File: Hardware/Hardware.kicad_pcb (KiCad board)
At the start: 2 copper layers, 68 parts, among them J1 LLINEIN, J2 RLINEIN, J3 MICIN, J4 Raspberry_Pi_2_3, J5 LOUT, J6 ROUT, J7 LHPOUT, J8 RHPOUT, SW1 JS5208, U1 MCP3004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

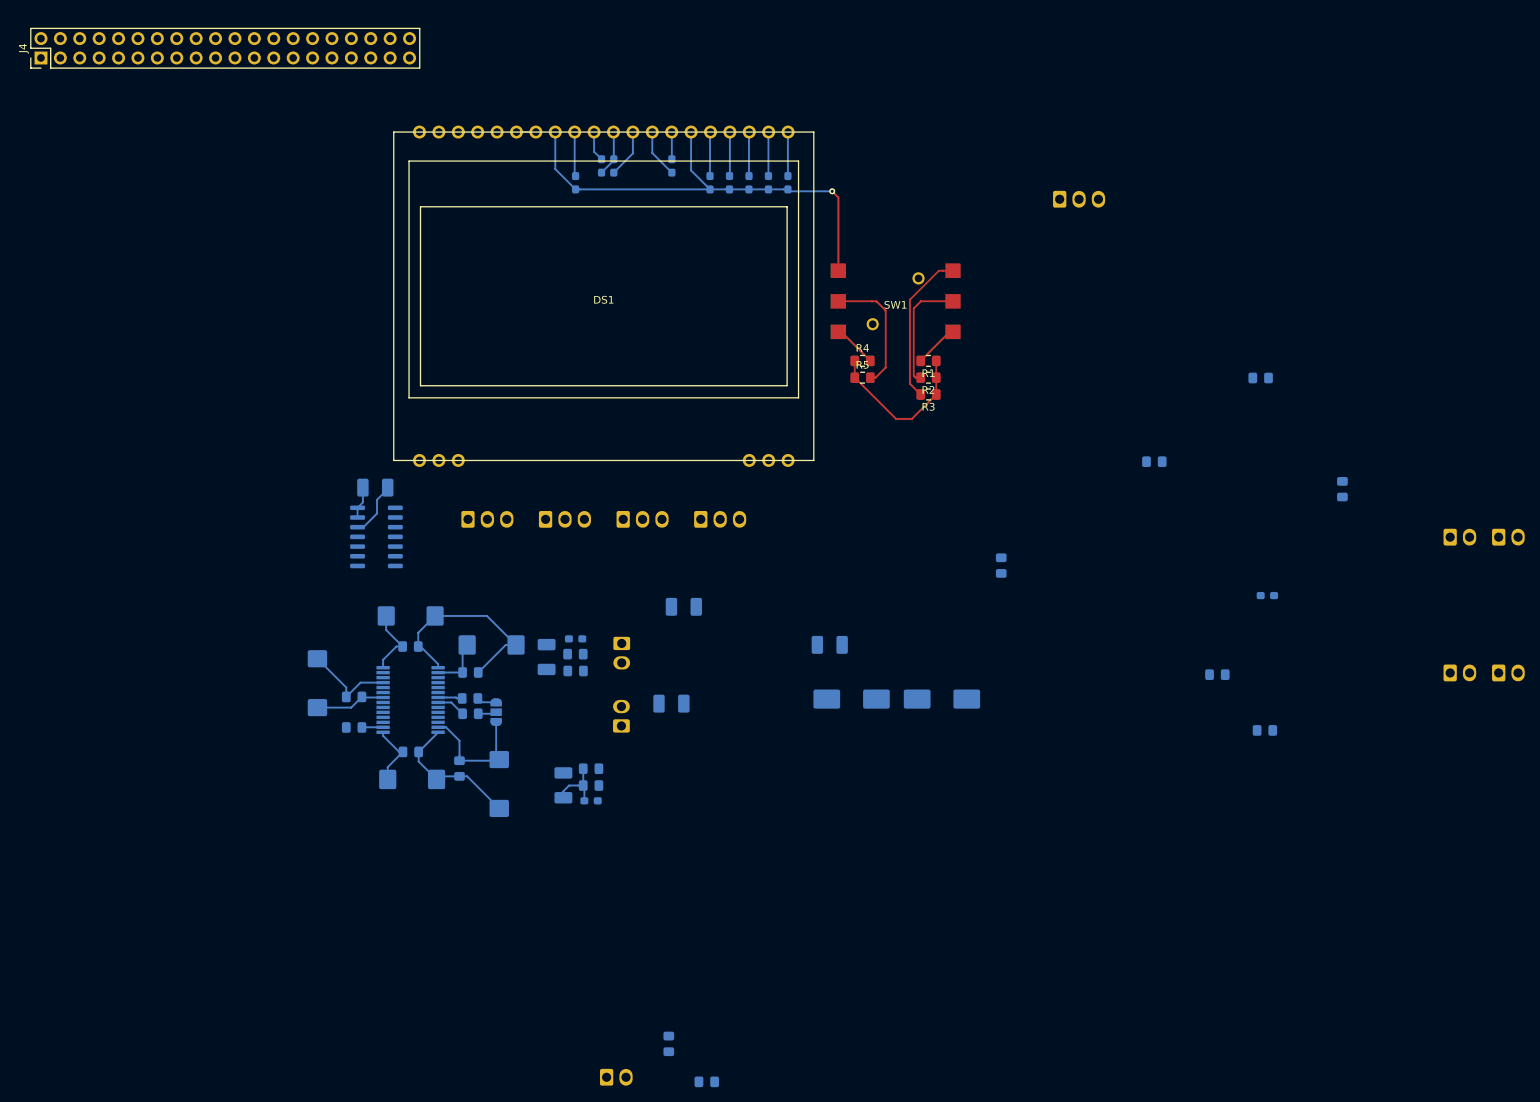
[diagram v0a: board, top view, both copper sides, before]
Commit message: Began layout and routing of PCB, generated files to allow use of FreeRouting
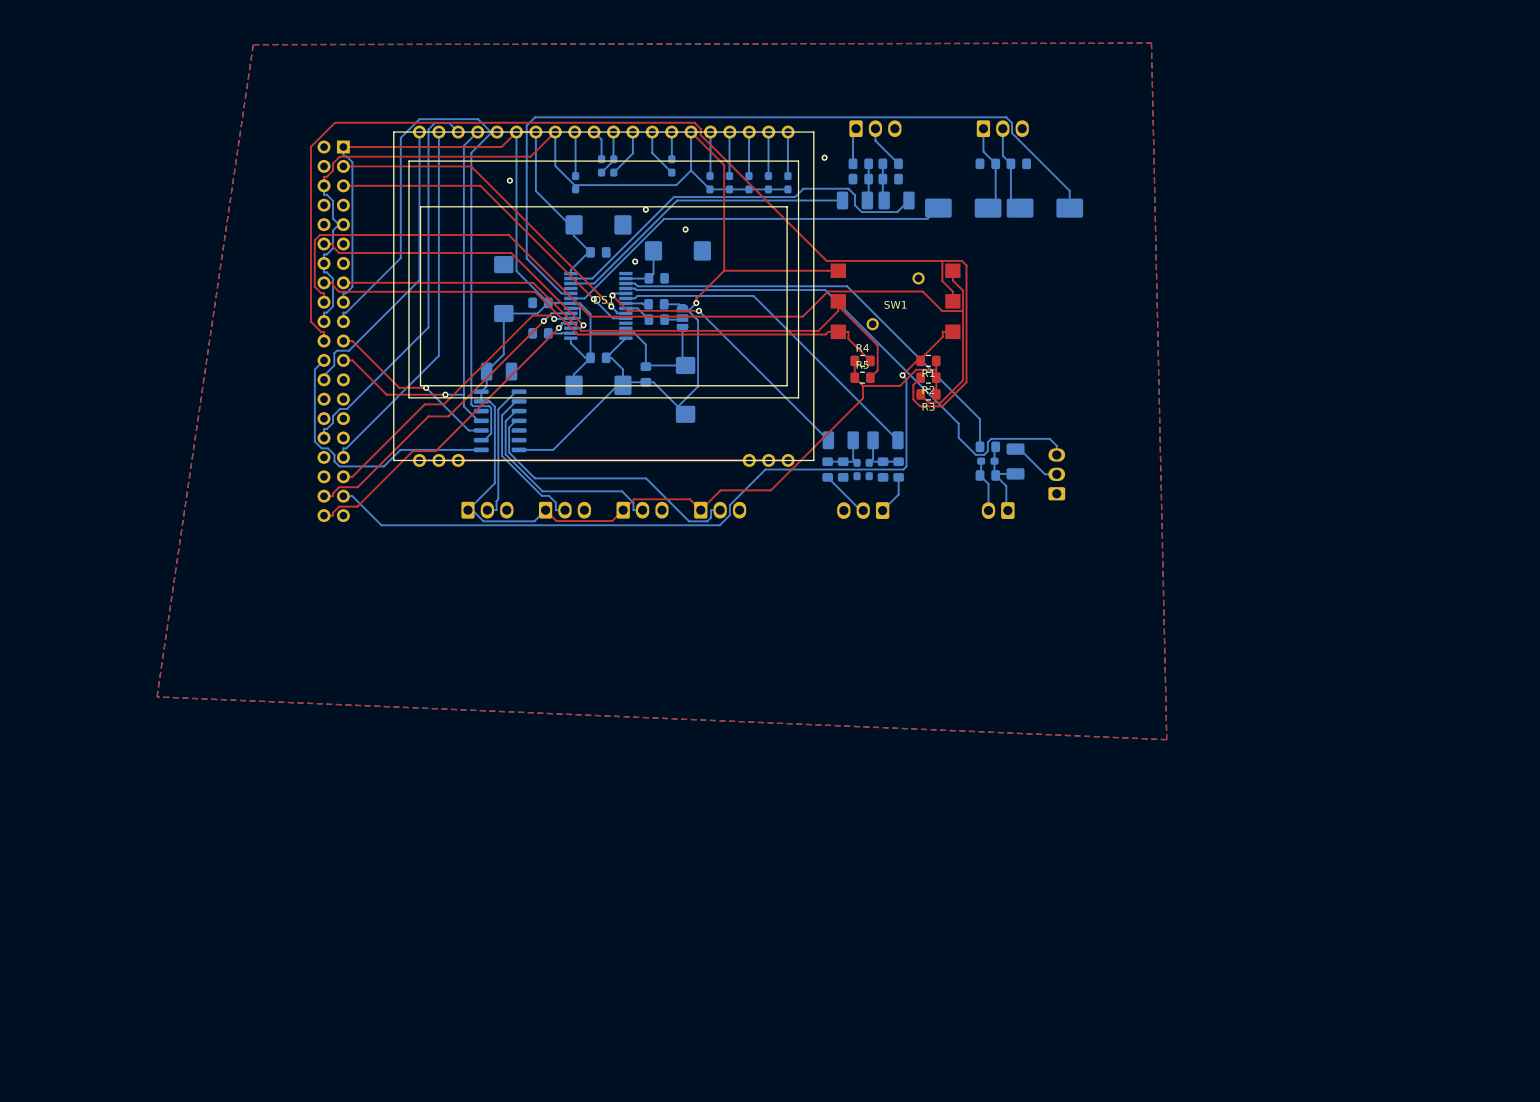
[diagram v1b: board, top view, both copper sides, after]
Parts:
- removed J6: ROUT, Connector_Molex:Molex_KK-254_AE-6410-02A_1x02_P2.54mm_Vertical
- removed J7: LHPOUT, Connector_Molex:Molex_KK-254_AE-6410-02A_1x02_P2.54mm_Vertical
- removed J8: RHPOUT, Connector_Molex:Molex_KK-254_AE-6410-02A_1x02_P2.54mm_Vertical
- J1: value LLINEIN -> LINEIN; footprint Connector_Molex:Molex_KK-254_AE-6410-02A_1x02_P2.54mm_Vertical -> Connector_Molex:Molex_KK-254_AE-6410-03A_1x03_P2.54mm_Vertical
- J2: value RLINEIN -> MICIN
- J3: value MICIN -> Raspberry_Pi_2_3; footprint Connector_Molex:Molex_KK-254_AE-6410-02A_1x02_P2.54mm_Vertical -> Connector_PinHeader_2.54mm:PinHeader_2x20_P2.54mm_Vertical
- J4: value Raspberry_Pi_2_3 -> LOUT; footprint Connector_PinHeader_2.54mm:PinHeader_2x20_P2.54mm_Vertical -> Connector_Molex:Molex_KK-254_AE-6410-03A_1x03_P2.54mm_Vertical; moved to B.Cu
- J5: value LOUT -> HPOUT; footprint Connector_Molex:Molex_KK-254_AE-6410-02A_1x02_P2.54mm_Vertical -> Connector_Molex:Molex_KK-254_AE-6410-03A_1x03_P2.54mm_Vertical
- moved J3 126.6 mm to (76.4, 33.8), turned to 180 degrees
- moved J4 107.1 mm to (143.5, 31.4), turned to 0 degrees
- moved R11 90.9 mm to (160.8, 73.1), turned to 180 degrees
- moved R16 87.2 mm to (148.1, 38.0)
- moved R6 85.3 mm to (160.8, 76.8), turned to 180 degrees
- moved J5 81.2 mm to (160.2, 31.4)
- moved R15 79.9 mm to (144.1, 38.0), turned to 180 degrees
- moved R20 72.9 mm to (148.1, 36.0), turned to 180 degrees
- moved C27 70.1 mm to (143.4, 40.8)
- moved C30 69.1 mm to (168.2, 41.8), turned to 180 degrees
- moved C29 64.3 mm to (157.6, 41.8)
- moved C15 61.8 mm to (147.4, 72.2), turned to 180 degrees
- moved C28 60.0 mm to (148.8, 40.8), turned to 180 degrees
- moved C21 57.2 mm to (109.8, 47.6)
- moved U2 57.2 mm to (109.8, 54.6)
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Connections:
- J1 pad 2: GNDA -> Net-(J1-Pad2)
- J2 pad 1: Net-(J2-Pad1) -> Net-(C11-Pad1)
- J3 pad 1: Net-(C11-Pad1) -> +3V3
- J3 pad 2: GNDA -> Net-(J3-Pad2)
- J4 pad 1: +3V3 -> Net-(J4-Pad1)
- J4 pad 3: /CODEC_SDA -> GNDA
- J5 pad 1: Net-(J5-Pad1) -> Net-(C29-Pad2)
- J5 pad 2: GNDA -> Net-(C30-Pad2)
- R19 pad 1: Net-(J5-Pad1) -> Net-(J4-Pad1)
- R20 pad 1: Net-(J6-Pad1) -> Net-(J4-Pad2)
- R8 pad 2: Net-(J2-Pad1) -> Net-(J1-Pad2)
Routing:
- net +3V3: track 70.8 -> 254.3 mm
- net /CTRLRIGHT: track 15.4 -> 154.7 mm
- net GNDD: track 83.1 -> 195.4 mm
- net /RHPOUT: track 0.00 -> 103.6 mm
- net /CTRLUP: track 20.2 -> 122.9 mm
- net /CTRLDOWN: track 5.80 -> 101.0 mm, vias 0 -> 1
- net /DISP_MOSI: track 0.00 -> 86.2 mm
- net /CTRLPUSH: track 5.77 -> 76.8 mm
- net /MICIN: track 0.00 -> 69.6 mm
- net /CTRLLEFT: track 16.7 -> 81.6 mm
- net /DISP_SCK: track 0.00 -> 57.4 mm, vias 0 -> 1
- net /MICBIAS: track 0.00 -> 57.3 mm
- net /LHPOUT: track 0.00 -> 53.0 mm
- net /ROUT: track 0.00 -> 51.8 mm
- net /DISP_MODE: track 0.00 -> 51.6 mm
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- added copper zone on B.Cu, net GNDA
- added copper zone on F.Cu, net GNDA

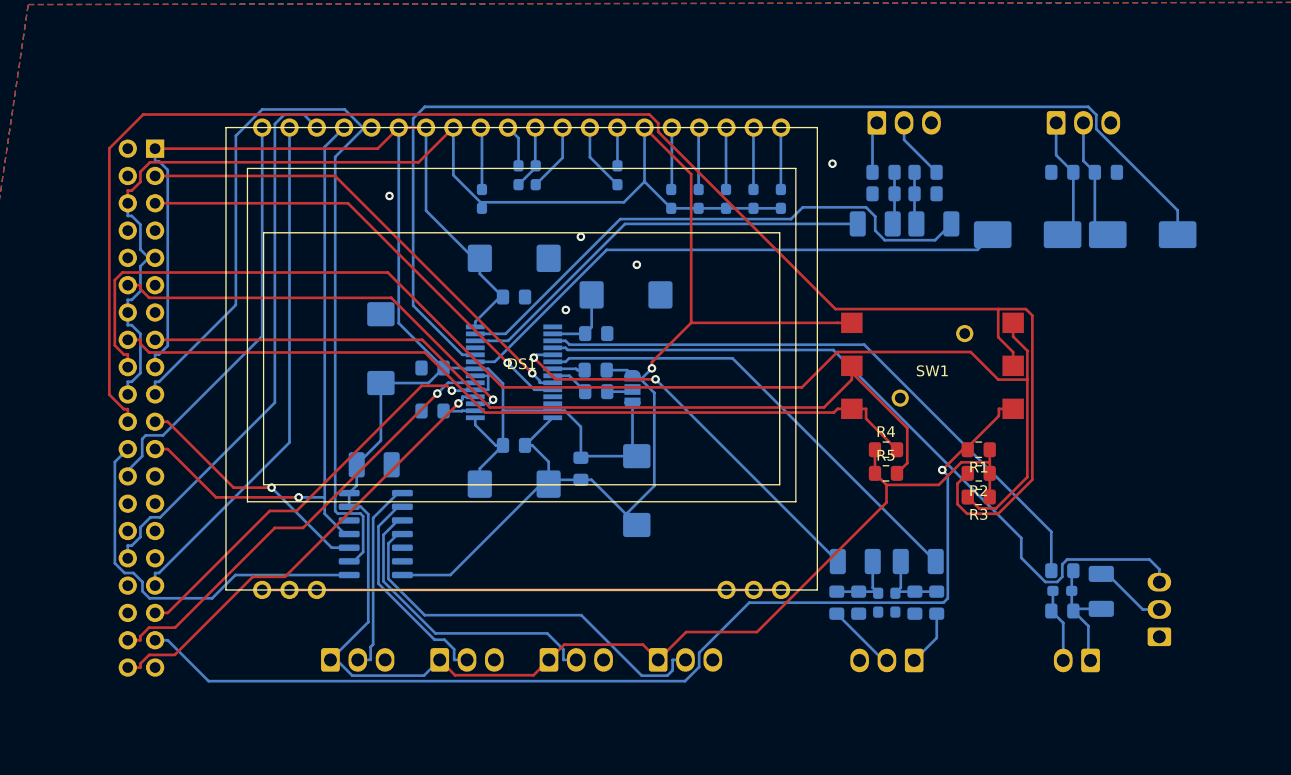
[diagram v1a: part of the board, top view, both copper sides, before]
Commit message: Routed main PCB
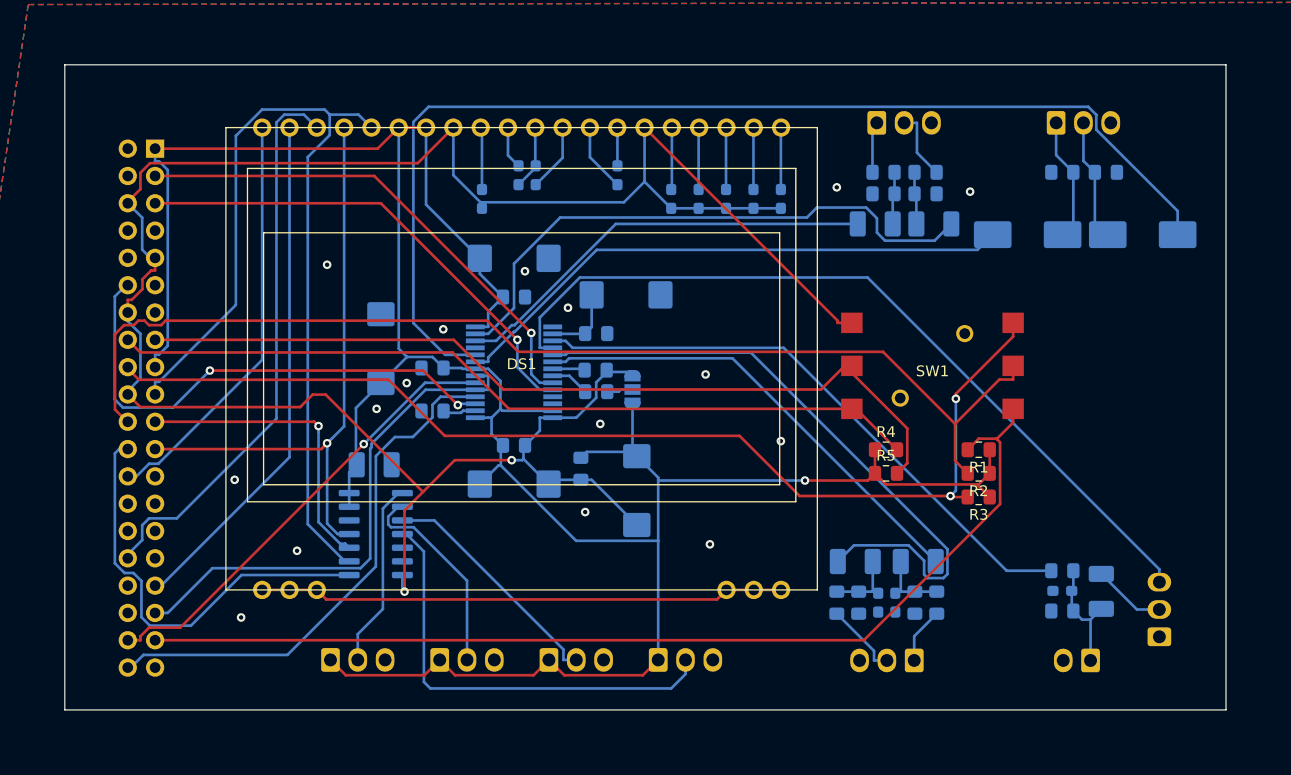
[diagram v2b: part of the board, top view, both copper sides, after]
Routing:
- net /CTRLRIGHT: track 154.7 -> 105.1 mm
- net /RLINEIN: track 38.0 -> 59.7 mm, vias 2 -> 0
- net /CTRLUP: track 122.9 -> 101.7 mm, vias 0 -> 2
- net GNDD: track 195.4 -> 209.8 mm, vias 1 -> 2
- net /BCLK: track 40.4 -> 47.9 mm, vias 1 -> 2
- net GNDA: track 6.99 -> 0.00 mm, vias 5 -> 16
- net /DACDAT: track 43.1 -> 49.4 mm, vias 1 -> 0
- net /CTRLC: track 28.2 -> 22.1 mm
- net /MICIN: track 69.6 -> 75.6 mm
- net /LRC: track 42.5 -> 48.3 mm, vias 1 -> 0
- net /MISO: track 22.9 -> 28.1 mm
- net /CTRLDOWN: track 101.0 -> 96.6 mm, vias 1 -> 0
- net /~CS~: track 35.7 -> 39.7 mm
- net /CTRLD: track 37.5 -> 41.3 mm
- net /ROUT: track 51.8 -> 54.3 mm
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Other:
- board outline added: 108 x 60 mm
